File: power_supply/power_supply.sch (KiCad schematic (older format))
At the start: 45 parts, among them J1 Conn_01x04_Male, J2 Conn_01x03_Male, J3 Conn_01x03_Male, J4 Conn_01x03_Male, U1 LM7815_TO220, U2 LM7915_TO220, U3 LM7805_TO220

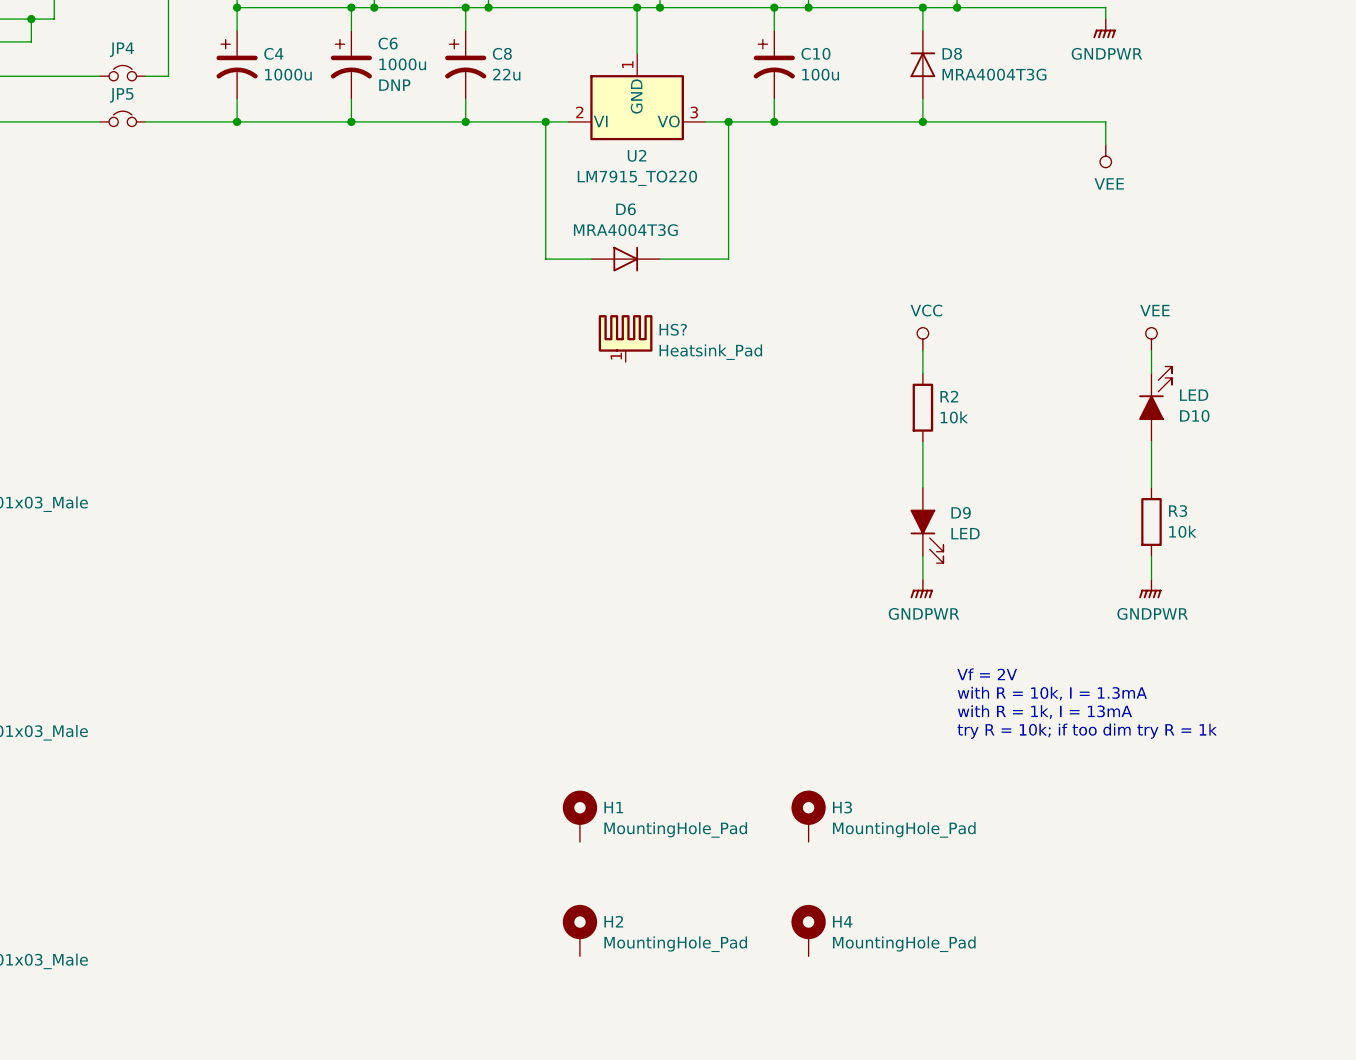
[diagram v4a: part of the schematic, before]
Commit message: update footprints for mounting holes (8-32 clearance)
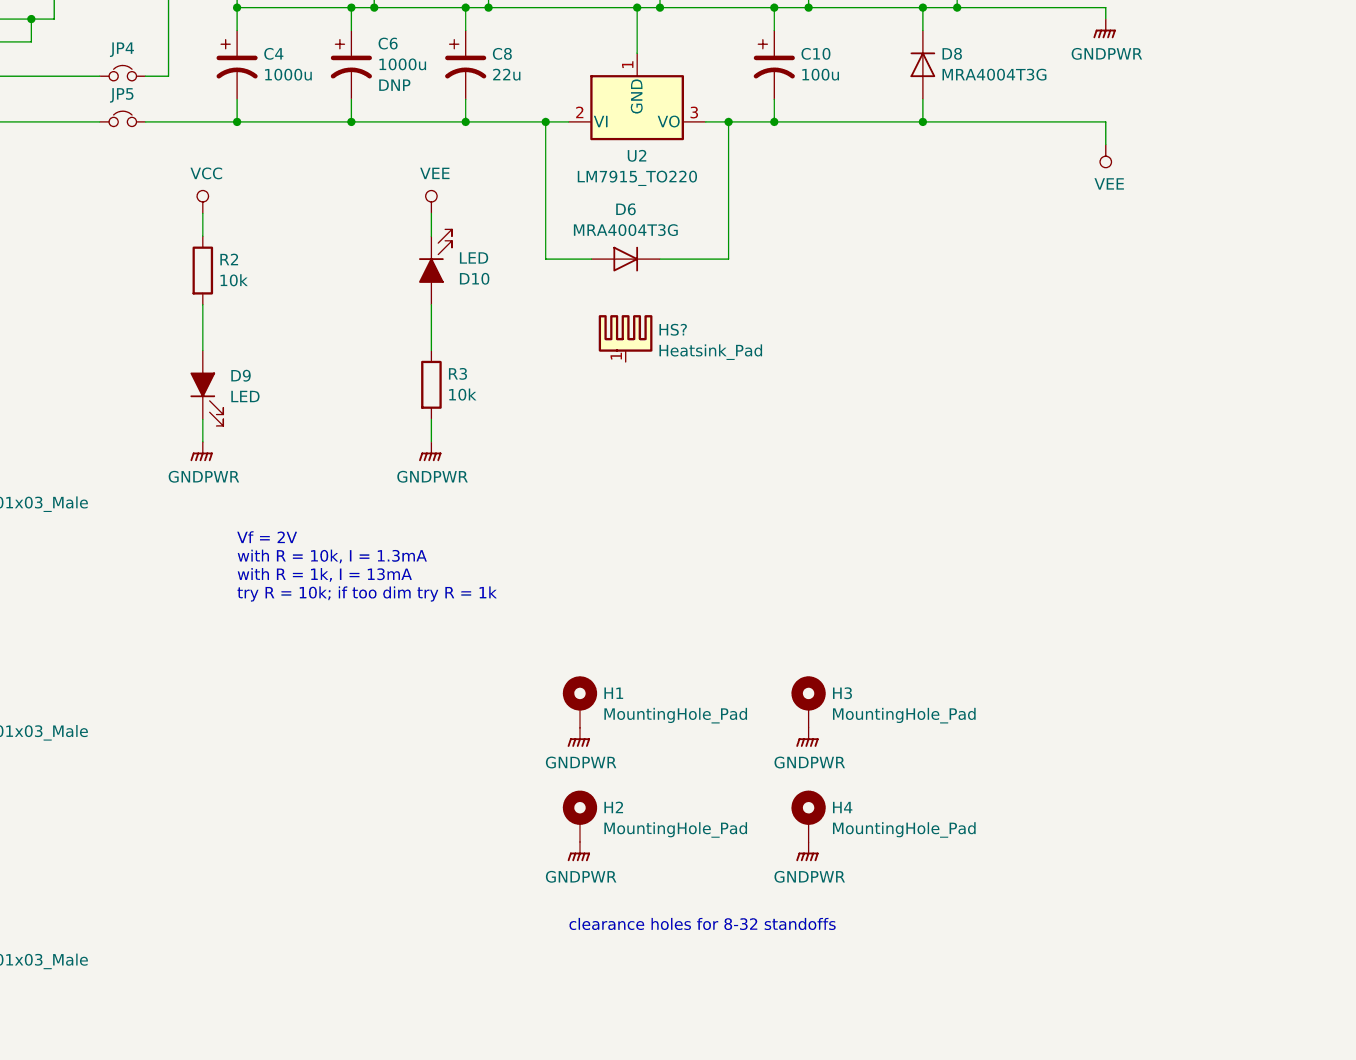
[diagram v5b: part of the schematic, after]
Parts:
- removed H2: MountingHole_Pad, MountingHole:MountingHole_4.3mm_M4_Pad, symbol Mechanical:MountingHole_Pad
- added H1: MountingHole_Pad, MountingHole:MountingHole_4.5mm_Pad, symbol Mechanical:MountingHole_Pad
- H2: renamed from H1; footprint MountingHole:MountingHole_4.3mm_M4_Pad -> MountingHole:MountingHole_4.5mm_Pad
- H3, H4: footprint MountingHole:MountingHole_4.3mm_M4_Pad -> MountingHole:MountingHole_4.5mm_Pad
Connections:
- net GNDPWR: now also H2.1, H3.1, H4.1, H1.1
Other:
- note added: "clearance holes for 8-32 standoffs"
- moved on the sheet: D10, D9, R2, R3
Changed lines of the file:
@@
 L Device:R R3
 U 1 1 5C5B0DBB
-P 9500 4750
-F 0 "R3" H 9570 4796 50  0000 L CNN
-F 1 "10k" H 9570 4705 50  0000 L CNN
-F 2 "Resistor_SMD:R_0603_1608Metric_Pad1.05x0.95mm_HandSolder" V 9430 4750 50  0001 C CNN
-F 3 "~" H 9500 4750 50  0001 C CNN
-	1    9500 4750
+P 6350 4150
+F 0 "R3" H 6420 4196 50  0000 L CNN
+F 1 "10k" H 6420 4105 50  0000 L CNN
+F 2 "Resistor_SMD:R_0603_1608Metric_Pad1.05x0.95mm_HandSolder" V 6280 4150 50  0001 C CNN
+F 3 "~" H 6350 4150 50  0001 C CNN
+	1    6350 4150
 	1    0    0    -1
 $EndComp
@@
 L power:GNDPWR #PWR0104
 U 1 1 5C9CF199
-P 8500 5000
-F 0 "#PWR0104" H 8500 4800 50  0001 C CNN
-F 1 "GNDPWR" H 8504 4846 50  0000 C CNN
-F 2 "" H 8500 4950 50  0001 C CNN
-F 3 "" H 8500 4950 50  0001 C CNN
-	1    8500 5000
+P 5350 4400
+F 0 "#PWR0104" H 5350 4200 50  0001 C CNN
+F 1 "GNDPWR" H 5354 4246 50  0000 C CNN
+F 2 "" H 5350 4350 50  0001 C CNN
+F 3 "" H 5350 4350 50  0001 C CNN
+	1    5350 4400
 	1    0    0    -1
 $EndComp
@@
 L power:GNDPWR #PWR0105
 U 1 1 5C9CF844
-P 9500 5000
-F 0 "#PWR0105" H 9500 4800 50  0001 C CNN
-F 1 "GNDPWR" H 9504 4846 50  0000 C CNN
-F 2 "" H 9500 4950 50  0001 C CNN
-F 3 "" H 9500 4950 50  0001 C CNN
-	1    9500 5000
+P 6350 4400
+F 0 "#PWR0105" H 6350 4200 50  0001 C CNN
+F 1 "GNDPWR" H 6354 4246 50  0000 C CNN
+F 2 "" H 6350 4350 50  0001 C CNN
+F 3 "" H 6350 4350 50  0001 C CNN
+	1    6350 4400
 	1    0    0    -1
 $EndComp
@@
 L power:VEE #PWR0106
 U 1 1 5C9D0258
-P 9500 4000
-F 0 "#PWR0106" H 9500 3850 50  0001 C CNN
-F 1 "VEE" H 9517 4173 50  0000 C CNN
-F 2 "" H 9500 4000 50  0001 C CNN
-F 3 "" H 9500 4000 50  0001 C CNN
-	1    9500 4000
+P 6350 3400
+F 0 "#PWR0106" H 6350 3250 50  0001 C CNN
+F 1 "VEE" H 6367 3573 50  0000 C CNN
+F 2 "" H 6350 3400 50  0001 C CNN
+F 3 "" H 6350 3400 50  0001 C CNN
+	1    6350 3400
 	1    0    0    -1
 $EndComp
@@
 L power:VCC #PWR0107
 U 1 1 5C9D0B19
-P 8500 4000
-F 0 "#PWR0107" H 8500 3850 50  0001 C CNN
-F 1 "VCC" H 8517 4173 50  0000 C CNN
-F 2 "" H 8500 4000 50  0001 C CNN
-F 3 "" H 8500 4000 50  0001 C CNN
-	1    8500 4000
-	1    0    0    -1
-$EndComp
-Wire Wire Line
-	9500 4000 9500 4100
-Wire Wire Line
-	9500 4400 9500 4600
-Wire Wire Line
-	9500 4900 9500 5000
-Text Notes 8650 5700 0    50   ~ 0
+P 5350 3400
+F 0 "#PWR0107" H 5350 3250 50  0001 C CNN
+F 1 "VCC" H 5367 3573 50  0000 C CNN
+F 2 "" H 5350 3400 50  0001 C CNN
+F 3 "" H 5350 3400 50  0001 C CNN
+	1    5350 3400
+	1    0    0    -1
+$EndComp
+Wire Wire Line
+	6350 3400 6350 3500
+Wire Wire Line
+	6350 3800 6350 4000
+Wire Wire Line
+	6350 4300 6350 4400
+Text Notes 5500 5100 0    50   ~ 0
 Vf = 2V\nwith R = 10k, I = 1.3mA\nwith R = 1k, I = 13mA\ntry R = 10k; if too dim try R = 1k
 $Comp
 L Device:LED_ALT D10
 U 1 1 5CA21F88
-P 9500 4250
-F 0 "D10" V 9538 4132 50  0000 R CNN
-F 1 "LED" V 9447 4132 50  0000 R CNN
-F 2 "LED_SMD:LED_0603_1608Metric" H 9500 4250 50  0001 C CNN
-F 3 "http://optoelectronics.liteon.com/upload/download/DS22-2000-223/LTST-C191KRKT.PDF" H 9500 4250 50  0001 C CNN
-F 4 "Lite-On" H 9500 4250 50  0001 C CNN "Manufacturer"
-F 5 "LTST-C191KRKT" H 9500 4250 50  0001 C CNN "Manufacturer PN"
-F 6 "Digikey" H 9500 4250 50  0001 C CNN "Distributor"
-F 7 "160-1447-1-ND" H 9500 4250 50  0001 C CNN "Distributor PN"
-F 8 "https://www.digikey.com/product-detail/en/lite-on-inc/LTST-C191KRKT/160-1447-1-ND/386836" H 9500 4250 50  0001 C CNN "URL"
-F 9 "0.29" H 9500 4250 50  0001 C CNN "Unit Price"
-	1    9500 4250
+P 6350 3650
+F 0 "D10" V 6388 3532 50  0000 R CNN
+F 1 "LED" V 6297 3532 50  0000 R CNN
+F 2 "LED_SMD:LED_0603_1608Metric" H 6350 3650 50  0001 C CNN
+F 3 "http://optoelectronics.liteon.com/upload/download/DS22-2000-223/LTST-C191KRKT.PDF" H 6350 3650 50  0001 C CNN
+F 4 "Lite-On" H 6350 3650 50  0001 C CNN "Manufacturer"
+F 5 "LTST-C191KRKT" H 6350 3650 50  0001 C CNN "Manufacturer PN"
+F 6 "Digikey" H 6350 3650 50  0001 C CNN "Distributor"
+F 7 "160-1447-1-ND" H 6350 3650 50  0001 C CNN "Distributor PN"
+F 8 "https://www.digikey.com/product-detail/en/lite-on-inc/LTST-C191KRKT/160-1447-1-ND/386836" H 6350 3650 50  0001 C CNN "URL"
+F 9 "0.29" H 6350 3650 50  0001 C CNN "Unit Price"
+	1    6350 3650
 	0    -1   1    0
 $EndComp
@@
 	1200 1550 1900 1550
 Wire Wire Line
-	8500 4900 8500 5000
-Wire Wire Line
-	8500 4400 8500 4600
-Wire Wire Line
-	8500 4000 8500 4100
+	5350 4300 5350 4400
+Wire Wire Line
+	5350 3800 5350 4000
+Wire Wire Line
+	5350 3400 5350 3500
 $Comp
 L Device:R R2
 U 1 1 5C4110E7
-P 8500 4250
-F 0 "R2" H 8570 4296 50  0000 L CNN
-F 1 "10k" H 8570 4205 50  0000 L CNN
-F 2 "Resistor_SMD:R_0603_1608Metric_Pad1.05x0.95mm_HandSolder" V 8430 4250 50  0001 C CNN
-F 3 "~" H 8500 4250 50  0001 C CNN
-	1    8500 4250
+P 5350 3650
+F 0 "R2" H 5420 3696 50  0000 L CNN
+F 1 "10k" H 5420 3605 50  0000 L CNN
+F 2 "Resistor_SMD:R_0603_1608Metric_Pad1.05x0.95mm_HandSolder" V 5280 3650 50  0001 C CNN
+F 3 "~" H 5350 3650 50  0001 C CNN
+	1    5350 3650
 	1    0    0    -1
 $EndComp
@@
 L Device:LED_ALT D9
 U 1 1 5C40C321
-P 8500 4750
-F 0 "D9" V 8538 4632 50  0000 R CNN
-F 1 "LED" V 8447 4632 50  0000 R CNN
-F 2 "LED_SMD:LED_0603_1608Metric" H 8500 4750 50  0001 C CNN
-F 3 "http://optoelectronics.liteon.com/upload/download/DS22-2000-223/LTST-C191KRKT.PDF" H 8500 4750 50  0001 C CNN
-F 4 "Lite-On" H 8500 4750 50  0001 C CNN "Manufacturer"
-F 5 "LTST-C191KRKT" H 8500 4750 50  0001 C CNN "Manufacturer PN"
-F 6 "Digikey" H 8500 4750 50  0001 C CNN "Distributor"
-F 7 "160-1447-1-ND" H 8500 4750 50  0001 C CNN "Distributor PN"
-F 8 "https://www.digikey.com/product-detail/en/lite-on-inc/LTST-C191KRKT/160-1447-1-ND/386836" H 8500 4750 50  0001 C CNN "URL"
-F 9 "0.29" H 8500 4750 50  0001 C CNN "Unit Price"
-	1    8500 4750
+P 5350 4150
+F 0 "D9" V 5388 4032 50  0000 R CNN
+F 1 "LED" V 5297 4032 50  0000 R CNN
+F 2 "LED_SMD:LED_0603_1608Metric" H 5350 4150 50  0001 C CNN
+F 3 "http://optoelectronics.liteon.com/upload/download/DS22-2000-223/LTST-C191KRKT.PDF" H 5350 4150 50  0001 C CNN
+F 4 "Lite-On" H 5350 4150 50  0001 C CNN "Manufacturer"
+F 5 "LTST-C191KRKT" H 5350 4150 50  0001 C CNN "Manufacturer PN"
+F 6 "Digikey" H 5350 4150 50  0001 C CNN "Distributor"
+F 7 "160-1447-1-ND" H 5350 4150 50  0001 C CNN "Distributor PN"
+F 8 "https://www.digikey.com/product-detail/en/lite-on-inc/LTST-C191KRKT/160-1447-1-ND/386836" H 5350 4150 50  0001 C CNN "URL"
+F 9 "0.29" H 5350 4150 50  0001 C CNN "Unit Price"
+	1    5350 4150
 	0    -1   -1   0
 $EndComp
@@
 $EndComp
 $Comp
-L Mechanical:MountingHole_Pad H1
+L Mechanical:MountingHole_Pad H2
 U 1 1 5CB49A9B
 P 7000 6050
-F 0 "H1" H 7100 6099 50  0000 L CNN
+F 0 "H2" H 7100 6099 50  0000 L CNN
 F 1 "MountingHole_Pad" H 7100 6008 50  0000 L CNN
-F 2 "MountingHole:MountingHole_4.3mm_M4_Pad" H 7000 6050 50  0001 C CNN
+F 2 "MountingHole:MountingHole_4.5mm_Pad" H 7000 6050 50  0001 C CNN
 F 3 "~" H 7000 6050 50  0001 C CNN
 	1    7000 6050
-	1    0    0    -1
-$EndComp
-$Comp
-L Mechanical:MountingHole_Pad H3
-U 1 1 5CB4A635
-P 8000 6050
-F 0 "H3" H 8100 6099 50  0000 L CNN
-F 1 "MountingHole_Pad" H 8100 6008 50  0000 L CNN
-F 2 "MountingHole:MountingHole_4.3mm_M4_Pad" H 8000 6050 50  0001 C CNN
-F 3 "~" H 8000 6050 50  0001 C CNN
-	1    8000 6050
-	1    0    0    -1
-$EndComp
-$Comp
-L Mechanical:MountingHole_Pad H4
-U 1 1 5CB4B51D
-P 8000 6550
-F 0 "H4" H 8100 6599 50  0000 L CNN
-F 1 "MountingHole_Pad" H 8100 6508 50  0000 L CNN
-F 2 "MountingHole:MountingHole_4.3mm_M4_Pad" H 8000 6550 50  0001 C CNN
-F 3 "~" H 8000 6550 50  0001 C CNN
-	1    8000 6550
-	1    0    0    -1
-$EndComp
-$Comp
-L Mechanical:MountingHole_Pad H2
-U 1 1 5CB4BFA5
-P 7000 6550
-F 0 "H2" H 7100 6599 50  0000 L CNN
-F 1 "MountingHole_Pad" H 7100 6508 50  0000 L CNN
-F 2 "MountingHole:MountingHole_4.3mm_M4_Pad" H 7000 6550 50  0001 C CNN
-F 3 "~" H 7000 6550 50  0001 C CNN
-	1    7000 6550
 	1    0    0    -1
 $EndComp
@@
 	1    0    0    -1
 $EndComp
+$Comp
+L power:GNDPWR #PWR?
+U 1 1 5CB598AE
+P 7000 6150
+F 0 "#PWR?" H 7000 5950 50  0001 C CNN
+F 1 "GNDPWR" H 7004 5996 50  0000 C CNN
+F 2 "" H 7000 6100 50  0001 C CNN
+F 3 "" H 7000 6100 50  0001 C CNN
+	1    7000 6150
+	1    0    0    -1
+$EndComp
+$Comp
+L Mechanical:MountingHole_Pad H1
+U 1 1 5CB5B46E
+P 7000 5550
+F 0 "H1" H 7100 5599 50  0000 L CNN
+F 1 "MountingHole_Pad" H 7100 5508 50  0000 L CNN
+F 2 "MountingHole:MountingHole_4.5mm_Pad" H 7000 5550 50  0001 C CNN
+F 3 "~" H 7000 5550 50  0001 C CNN
+	1    7000 5550
+	1    0    0    -1
+$EndComp
+$Comp
+L power:GNDPWR #PWR?
+U 1 1 5CB5B474
+P 7000 5650
+F 0 "#PWR?" H 7000 5450 50  0001 C CNN
+F 1 "GNDPWR" H 7004 5496 50  0000 C CNN
+F 2 "" H 7000 5600 50  0001 C CNN
+F 3 "" H 7000 5600 50  0001 C CNN
+	1    7000 5650
+	1    0    0    -1
+$EndComp
+$Comp
+L Mechanical:MountingHole_Pad H4
+U 1 1 5CB60C90
+P 8000 6050
+F 0 "H4" H 8100 6099 50  0000 L CNN
+F 1 "MountingHole_Pad" H 8100 6008 50  0000 L CNN
+F 2 "MountingHole:MountingHole_4.5mm_Pad" H 8000 6050 50  0001 C CNN
+F 3 "~" H 8000 6050 50  0001 C CNN
+	1    8000 6050
+	1    0    0    -1
+$EndComp
+$Comp
+L power:GNDPWR #PWR?
+U 1 1 5CB60C96
+P 8000 6150
+F 0 "#PWR?" H 8000 5950 50  0001 C CNN
+F 1 "GNDPWR" H 8004 5996 50  0000 C CNN
+F 2 "" H 8000 6100 50  0001 C CNN
+F 3 "" H 8000 6100 50  0001 C CNN
+	1    8000 6150
+	1    0    0    -1
+$EndComp
+$Comp
+L Mechanical:MountingHole_Pad H3
+U 1 1 5CB6616E
+P 8000 5550
+F 0 "H3" H 8100 5599 50  0000 L CNN
+F 1 "MountingHole_Pad" H 8100 5508 50  0000 L CNN
+F 2 "MountingHole:MountingHole_4.5mm_Pad" H 8000 5550 50  0001 C CNN
+F 3 "~" H 8000 5550 50  0001 C CNN
+	1    8000 5550
+	1    0    0    -1
+$EndComp
+$Comp
+L power:GNDPWR #PWR?
+U 1 1 5CB66174
+P 8000 5650
+F 0 "#PWR?" H 8000 5450 50  0001 C CNN
+F 1 "GNDPWR" H 8004 5496 50  0000 C CNN
+F 2 "" H 8000 5600 50  0001 C CNN
+F 3 "" H 8000 5600 50  0001 C CNN
+	1    8000 5650
+	1    0    0    -1
+$EndComp
+Text Notes 6950 6550 0    50   ~ 0
+clearance holes for 8-32 standoffs
 $EndSCHEMATC
